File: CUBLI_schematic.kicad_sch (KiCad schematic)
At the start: 4 parts

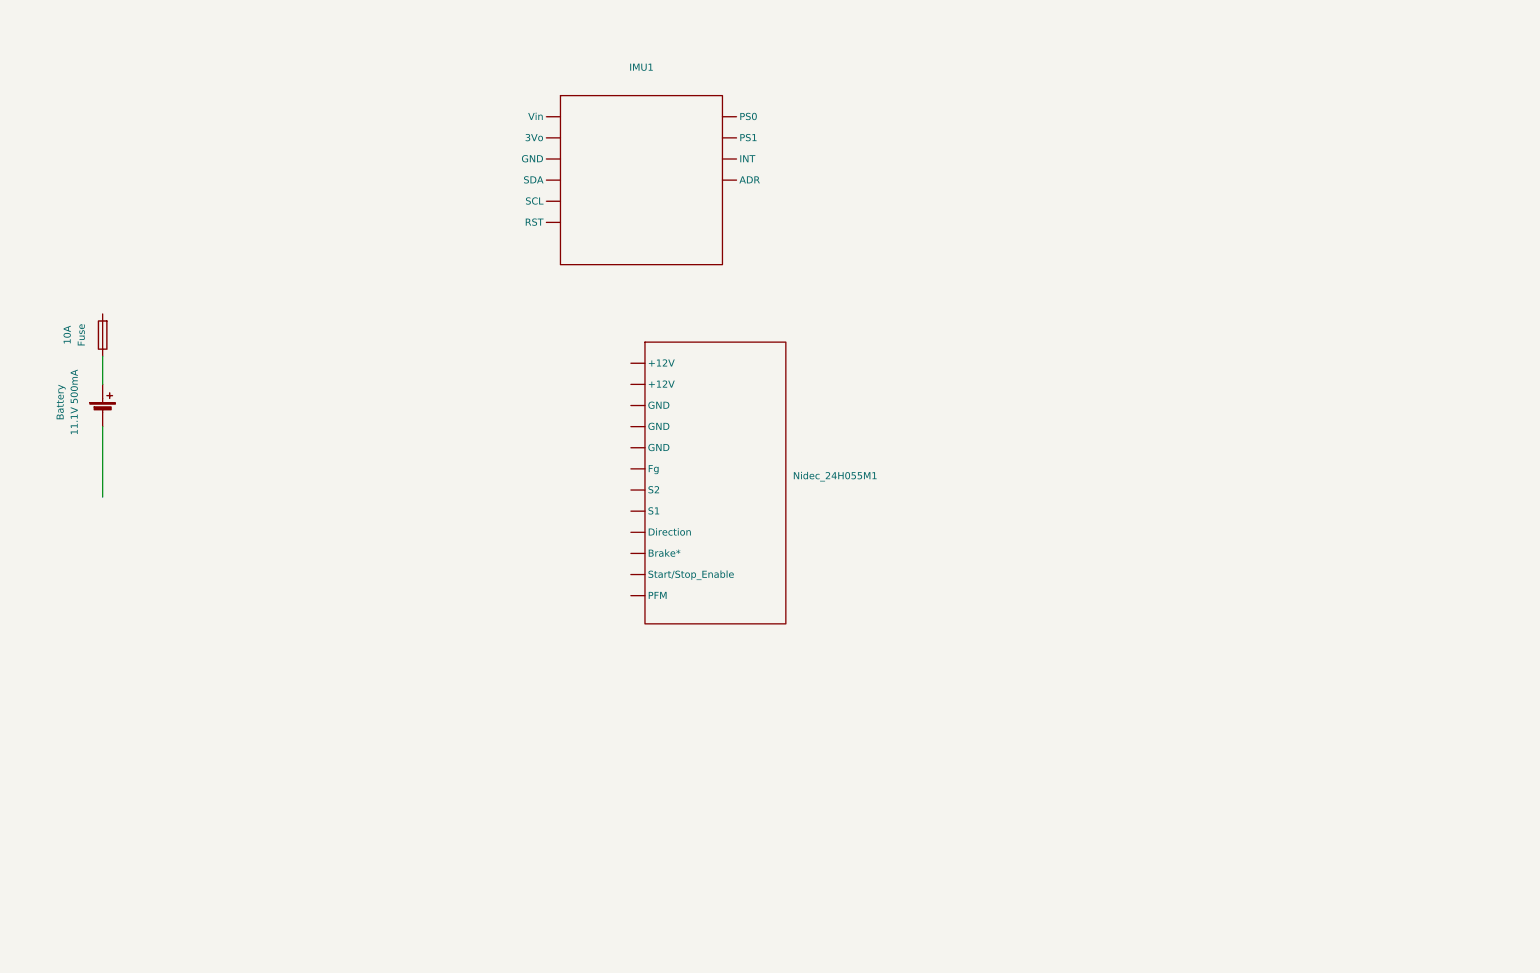
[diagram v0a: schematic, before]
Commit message: Finished wiring motors, power distribution, and IMU
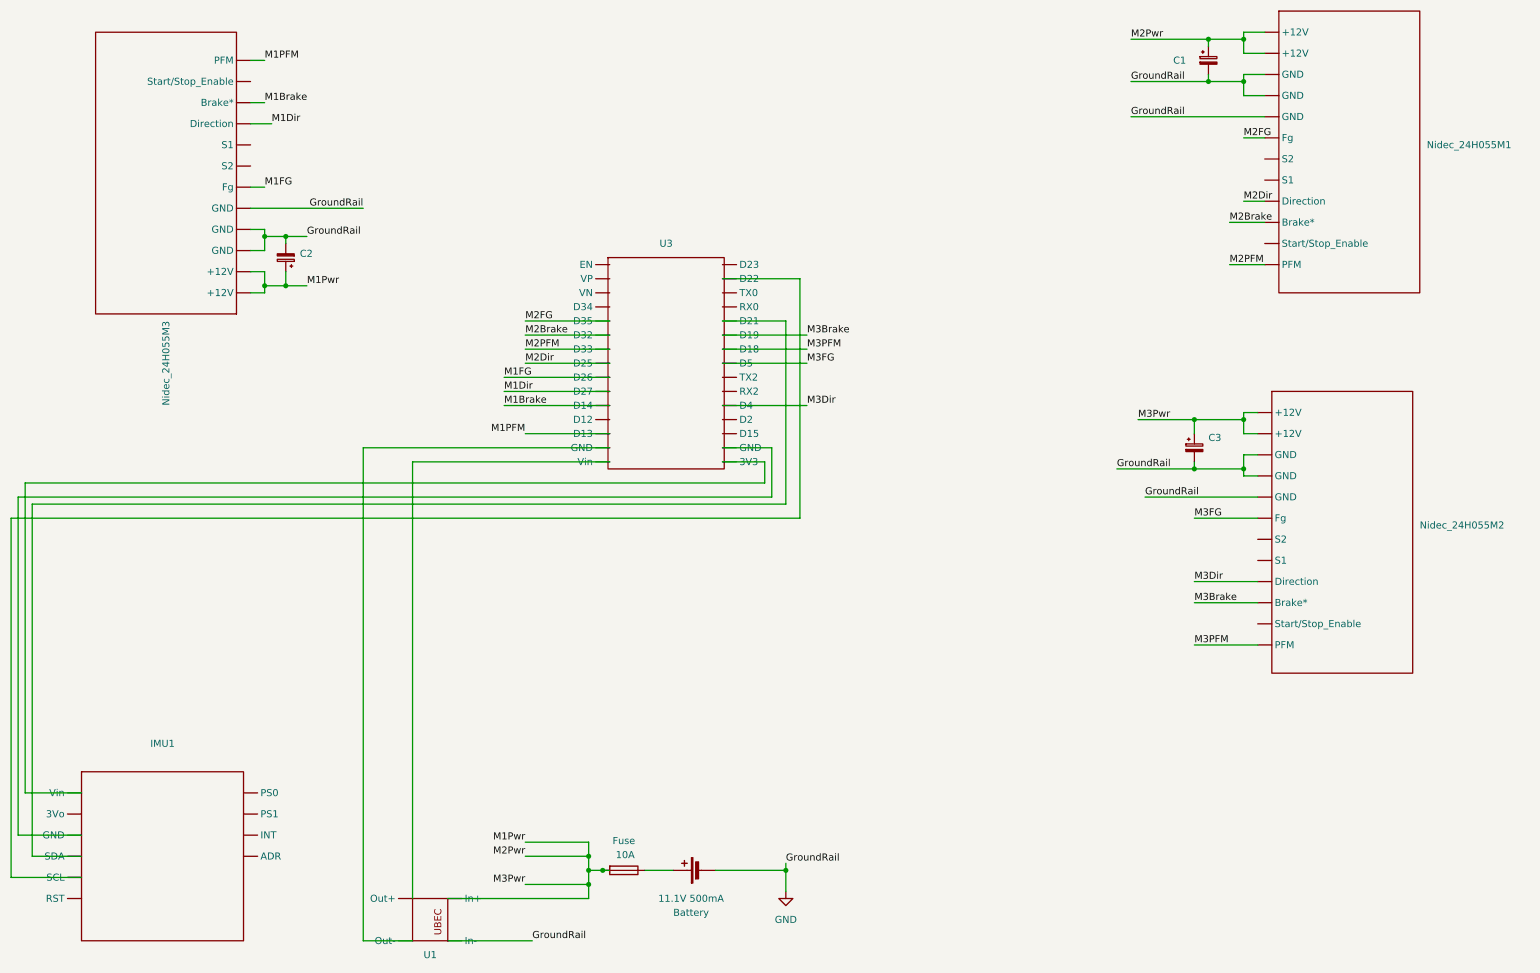
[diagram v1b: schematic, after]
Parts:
- added C1, C2, C3: C_Polarized_Small, symbol Device:C_Polarized_Small
- added Nidec_24H055M2, Nidec_24H055M3: (no value), symbol Nidec.Kicad:Nidec
- added U1: (no value), symbol CUBLI_Library:UBEC
- added U3: (no value), symbol CUBLI_Library:ESPReal
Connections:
- net M2PFM: now reaches Nidec_24H055M1. (PFM)
- net M2PFM: now also U3. (3V3)
- net GND: now reaches Battery.2 (-)
- net GND: now also Nidec_24H055M1. (PFM), C1.2, C2.2, C3.2, Nidec_24H055M2. (PFM), Nidec_24H055M3. (PFM), U1. (Out+)
- net M1Pwr: now reaches 10A.2
- net M1Pwr: now also Nidec_24H055M1. (PFM), C1.1, C2.1, C3.1, Nidec_24H055M2. (PFM), Nidec_24H055M3. (PFM), U1. (Out+)
- new net: U1. (Out+), U3. (3V3) (x2)
- new net: IMU1. (ADR), U3. (3V3) (x4)
- new net M1Brake: Nidec_24H055M3. (PFM), U3. (3V3)
- new net M1Dir: Nidec_24H055M3. (PFM), U3. (3V3)
- new net M1FG: Nidec_24H055M3. (PFM), U3. (3V3)
- new net M1PFM: Nidec_24H055M3. (PFM), U3. (3V3)
- new net M2Brake: Nidec_24H055M1. (PFM), U3. (3V3)
- new net M2Dir: Nidec_24H055M1. (PFM), U3. (3V3)
- new net M2FG: Nidec_24H055M1. (PFM), U3. (3V3)
- new net M3Brake: Nidec_24H055M2. (PFM), U3. (3V3)
- new net M3Dir: Nidec_24H055M2. (PFM), U3. (3V3)
- new net M3FG: Nidec_24H055M2. (PFM), U3. (3V3)
- new net M3PFM: Nidec_24H055M2. (PFM), U3. (3V3)
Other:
- moved on the sheet: 10A, Battery, IMU1, Nidec_24H055M1
